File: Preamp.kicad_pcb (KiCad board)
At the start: 2 copper layers, 285 x 74 mm, 169 parts, among them J1 Conn_01x03, J10 RCAJack, J11 XLR4BODYPIN, J12 XLR4BODYPIN, J13 XLR4BODYPIN, J14 RCAJack, J15 RCAJack, J16 RCAJack, J17 RCAJack, J18 RCAJack, J19 RCAJack, J2 Conn_01x02, J20 RCAJack, J21 RCAJack, J22 Jack-DC, J23 Conn_01x02, J24 Conn_01x02, J3 Conn_01x02, J4 RCAJack, J5 RCAJack, J6 Conn_01x01, J7 Conn_01x01, J8 Conn_01x01, J9 Conn_01x01, SW1 SW_SPST, SW2 SW_SPST, SW3 SW_SPST, U1 LM317, U2 LM337, U3 LM4562, U4 LM4562, U5 LM4562, U6 LM4562, U7 LM4562, U8 LM4562

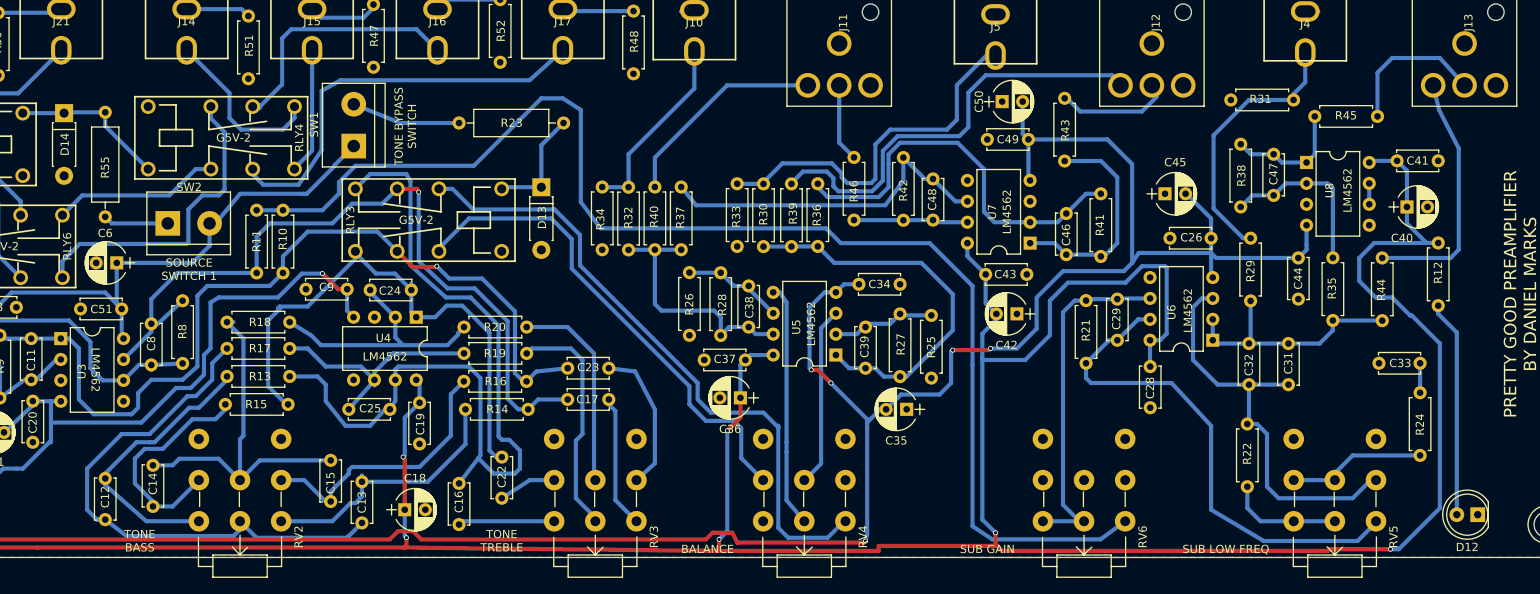
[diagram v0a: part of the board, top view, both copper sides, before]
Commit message: Changed balanced output to THAT1646
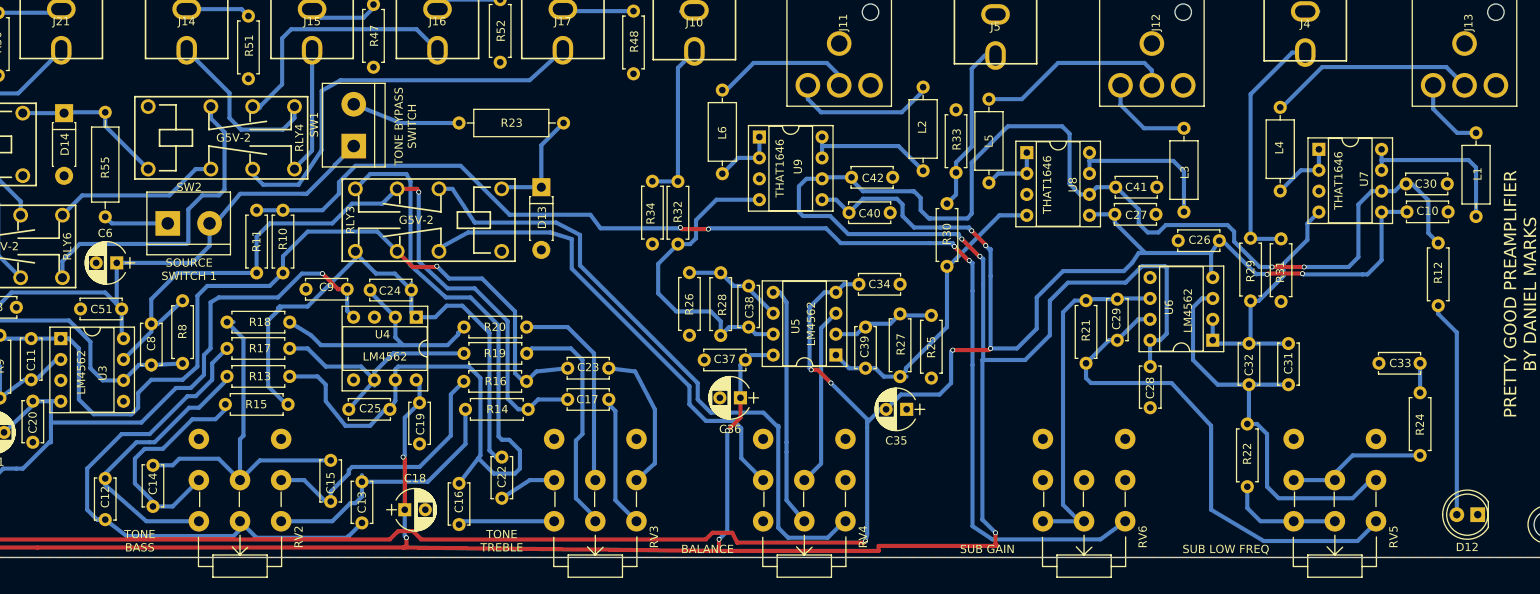
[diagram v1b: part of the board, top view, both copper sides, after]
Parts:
- removed C43, C44, C49: 100 nF, Capacitors_THT:C_Disc_D5.0mm_W2.5mm_P5.00mm
- removed C45, C50: 47 uF, Capacitors_THT:CP_Radial_D5.0mm_P2.50mm
- removed C46, C47, C48: 22 pF, Capacitors_THT:C_Disc_D5.0mm_W2.5mm_P5.00mm
- removed R35, R36, R37, R38, R41, R42: 10k, Resistors_THT:R_Axial_DIN0207_L6.3mm_D2.5mm_P7.62mm_Horizontal
- removed R39, R40, R43, R44, R45, R46: 100R, Resistors_THT:R_Axial_DIN0207_L6.3mm_D2.5mm_P7.62mm_Horizontal
- added C10: 100 nF, Capacitors_THT:C_Disc_D5.0mm_W2.5mm_P5.00mm, F.Cu at (278.0, 64.0)
- added C27: 100 nF, Capacitors_THT:C_Disc_D5.0mm_W2.5mm_P5.00mm, F.Cu at (242.5, 64.3)
- added C30: 100 nF, Capacitors_THT:C_Disc_D5.0mm_W2.5mm_P5.00mm, F.Cu at (277.9, 60.6)
- added L1: FB, Inductors_THT:L_Axial_L7.0mm_D3.3mm_P10.16mm_Horizontal_Fastron_MICC, F.Cu at (281.4, 54.4)
- added L2: FB, Inductors_THT:L_Axial_L7.0mm_D3.3mm_P10.16mm_Horizontal_Fastron_MICC, F.Cu at (214.2, 59.0)
- added L3: FB, Inductors_THT:L_Axial_L7.0mm_D3.3mm_P10.16mm_Horizontal_Fastron_MICC, F.Cu at (245.9, 64.0)
- added L4: FB, Inductors_THT:L_Axial_L7.0mm_D3.3mm_P10.16mm_Horizontal_Fastron_MICC, F.Cu at (257.6, 51.3)
- added L5: FB, Inductors_THT:L_Axial_L7.0mm_D3.3mm_P10.16mm_Horizontal_Fastron_MICC, F.Cu at (222.2, 50.3)
- added L6: FB, Inductors_THT:L_Axial_L7.0mm_D3.3mm_P10.16mm_Horizontal_Fastron_MICC, F.Cu at (189.8, 49.2)
- added U9: THAT1646, Housings_DIP:DIP-8_W7.62mm_Socket, F.Cu at (194.3, 54.9)
- C40, C42: value 47 uF -> 100 nF; footprint Capacitors_THT:CP_Radial_D5.0mm_P2.50mm -> Capacitors_THT:C_Disc_D5.0mm_W2.5mm_P5.00mm
- U3, U4, U5, U6: footprint Housings_DIP:DIP-8_W7.62mm -> Housings_DIP:DIP-8_W7.62mm_Socket
- U7, U8: value LM4562 -> THAT1646; footprint Housings_DIP:DIP-8_W7.62mm -> Housings_DIP:DIP-8_W7.62mm_Socket
- moved C40 62.8 mm to (210.2, 64.1), turned to 180 degrees
- moved U7 36.9 mm to (262.3, 56.4), turned to 0 degrees
- moved U8 34.0 mm to (226.8, 56.8)
- moved R33 31.4 mm to (218.2, 51.6), turned to 270 degrees
- moved C41 29.4 mm to (242.6, 61.0), turned to 180 degrees
- moved R31 25.2 mm to (257.7, 74.9), turned to 90 degrees
- moved C42 22.4 mm to (210.5, 59.8)
- moved R30 22.4 mm to (217.1, 63.0)
- moved R34 6.14 mm to (181.3, 67.9)
- moved R32 6.04 mm to (184.4, 60.3)
- moved C26 1.04 mm to (245.2, 67.5)
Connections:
- C40 pad 1: +15V -> GND
- C40 pad 2: GND -> -15V
- C41 pad 1: +15V -> GND
- C41 pad 2: GND -> +15V
- U7 pad 1: Net-(C46-Pad1) -> Net-(L4-Pad2)
- U7 pad 2: Net-(C46-Pad2) -> Net-(L4-Pad2)
- U7 pad 4: -15V -> Net-(C31-Pad1)
- U7 pad 5: GND -> -15V
- U7 pad 6: Net-(C48-Pad2) -> +15V
- U7 pad 7: Net-(C48-Pad1) -> Net-(L1-Pad2)
- U7 pad 8: +15V -> Net-(L1-Pad2)
- U8 pad 1: Net-(C47-Pad1) -> Net-(L5-Pad2)
- U8 pad 2: Net-(C47-Pad2) -> Net-(L5-Pad2)
- U8 pad 4: -15V -> Net-(C39-Pad1)
- U8 pad 5: GND -> -15V
- U8 pad 6: Net-(U8-Pad6) -> +15V
- U8 pad 7: Net-(U8-Pad6) -> Net-(L3-Pad1)
- U8 pad 8: +15V -> Net-(L3-Pad1)
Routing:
- net Net-(C46-Pad2): track 48.9 -> 0.00 mm
- net Net-(C48-Pad2): track 42.7 -> 0.00 mm
- net Net-(J12-Pad2): track 53.4 -> 11.3 mm
- net Net-(C46-Pad1): track 27.2 -> 0.00 mm
- net Net-(J5-Pad2): track 45.2 -> 22.3 mm
- net +15V: track 552.6 -> 574.5 mm, vias 7 -> 10
- net Net-(C47-Pad2): track 21.6 -> 0.00 mm
- net Net-(J13-Pad2): track 30.8 -> 9.29 mm
- net Net-(L1-Pad2): track 0.00 -> 20.4 mm
- net -15V: track 484.6 -> 504.9 mm, vias 8 -> 12
- net Net-(L3-Pad1): track 0.00 -> 19.5 mm
- net Net-(L2-Pad1): track 0.00 -> 16.1 mm
- net Net-(C47-Pad1): track 14.9 -> 0.00 mm
- net Net-(C48-Pad1): track 13.9 -> 0.00 mm
- net Net-(R10-Pad1): track 158.5 -> 147.1 mm, vias 0 -> 4
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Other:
- board text added: "THAT1646"

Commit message: Changed one input to be balanced
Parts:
- removed R48, R52: 10R, Resistors_THT:R_Axial_DIN0207_L6.3mm_D2.5mm_P7.62mm_Horizontal
- added C43: 100 nF, Capacitors_THT:C_Disc_D5.0mm_W2.5mm_P5.00mm, F.Cu at (186.1, 51.3)
- added C44: 100 nF, Capacitors_THT:C_Disc_D5.0mm_W2.5mm_P5.00mm, F.Cu at (214.5, 61.0)
- added C45: 100 nF, Capacitors_THT:C_Disc_D5.0mm_W2.5mm_P5.00mm, F.Cu at (195.9, 66.0)
- added C46: 100 nF, Capacitors_THT:C_Disc_D5.0mm_W2.5mm_P5.00mm, F.Cu at (191.5, 66.4)
- added C47: 220 uF, Capacitors_THT:CP_Radial_D7.5mm_P2.50mm, F.Cu at (177.1, 63.6)
- added C48: 220 uF, Capacitors_THT:CP_Radial_D7.5mm_P2.50mm, F.Cu at (197.6, 61.6)
- added C49: 47 uF, Capacitors_THT:CP_Radial_D5.0mm_P2.50mm, F.Cu at (95.8, 81.8)
- added C50: 47 uF, Capacitors_THT:CP_Radial_D5.0mm_P2.50mm, F.Cu at (87.3, 82.6)
- added C52: 47 uF, Capacitors_THT:CP_Radial_D5.0mm_P2.50mm, F.Cu at (87.4, 79.3)
- added C53: 47 uF, Capacitors_THT:CP_Radial_D5.0mm_P2.50mm, F.Cu at (95.8, 78.5)
- added C54: 100 pF, Capacitors_THT:C_Disc_D5.0mm_W2.5mm_P5.00mm, F.Cu at (144.5, 54.4)
- added C55: 100 pF, Capacitors_THT:C_Disc_D5.0mm_W2.5mm_P5.00mm, F.Cu at (168.5, 43.4)
- added C56: 100 pF, Capacitors_THT:C_Disc_D5.0mm_W2.5mm_P5.00mm, F.Cu at (152.9, 54.5)
- added C57: 100 pF, Capacitors_THT:C_Disc_D5.0mm_W2.5mm_P5.00mm, F.Cu at (165.4, 43.4)
- added J25: Conn_01x01, Connectors:1pin, F.Cu at (236.3, 54.4)
- added J26: Conn_01x01, Connectors:1pin, F.Cu at (185.0, 98.0)
- added J27: Conn_01x01, Connectors:1pin, F.Cu at (114.5, 49.0)
- added J28: Conn_01x01, Connectors:1pin, F.Cu at (107.0, 98.0)
- added JP1: INA134, Pin_Headers:Pin_Header_Straight_1x02_Pitch2.54mm, F.Cu at (179.1, 56.5)
- added JP2: INA134, Pin_Headers:Pin_Header_Straight_1x02_Pitch2.54mm, F.Cu at (199.5, 54.3)
- added R35: 10k, Resistors_THT:R_Axial_DIN0207_L6.3mm_D2.5mm_P7.62mm_Horizontal, F.Cu at (87.0, 102.5)
- added R36: 10k, Resistors_THT:R_Axial_DIN0207_L6.3mm_D2.5mm_P7.62mm_Horizontal, F.Cu at (94.5, 99.2)
- added U10: THAT1200, Housings_DIP:DIP-8_W7.62mm_Socket, F.Cu at (191.0, 63.4)
- added U11: THAT1200, Housings_DIP:DIP-8_W7.62mm_Socket, F.Cu at (211.1, 64.7)
- J16, J17: value RCAJack -> XLR4BODYPIN; footprint Preamp:RCAConnectorCommon -> Preamp:IOXLR3FEH
- R8, R9: value 22k -> 47k
- moved SW1 40.2 mm to (180.6, 74.6), turned to 180 degrees
- moved R32 36.6 mm to (220.9, 57.6)
- moved R34 36.5 mm to (217.8, 65.3)
- moved R30 32.3 mm to (248.9, 57.7)
- moved U9 31.1 mm to (225.1, 59.1)
- moved C40 30.8 mm to (241.0, 64.9)
- moved R33 30.7 mm to (245.8, 65.2), turned to 90 degrees
- moved C42 30.6 mm to (241.0, 61.6)
- moved L4 29.1 mm to (277.7, 72.3), turned to 180 degrees
- moved R23 29.0 mm to (182.4, 68.5), turned to 180 degrees
- moved U8 28.7 mm to (255.5, 58.4)
- moved C41 28.6 mm to (271.1, 62.8)
- moved C27 28.5 mm to (271.0, 65.9)
- moved L6 28.5 mm to (217.8, 54.2), turned to 0 degrees
- moved R29 26.6 mm to (280.6, 68.3), turned to 180 degrees
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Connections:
- C3 pad 1: LEFTIN -> Net-(C3-Pad1)
- C7 pad 1: RIGHTIN -> Net-(C50-Pad2)
- J16 pad 1: Net-(J16-Pad1) -> GND
- J16 pad 2: Net-(J16-Pad2) -> Net-(C56-Pad2)
- J17 pad 1: Net-(J17-Pad1) -> GND
- J17 pad 2: Net-(J17-Pad2) -> Net-(C57-Pad2)
- RLY4 pad 1: GND -> Net-(D14-Pad1)
- RLY4 pad 3: Net-(J16-Pad2) -> Net-(J14-Pad2)
- RLY4 pad 4: Net-(J14-Pad2) -> Net-(JP1-Pad1)
- RLY4 pad 5: Net-(D14-Pad1) -> GND
- RLY4 pad 7: Net-(J17-Pad2) -> Net-(J15-Pad2)
- RLY4 pad 8: Net-(J15-Pad2) -> Net-(JP2-Pad1)
- RV1 pad 1: LEFTIN -> Net-(R35-Pad1)
- RV1 pad 4: RIGHTIN -> Net-(R36-Pad2)
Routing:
- net -15V: track 504.9 -> 713.4 mm, vias 12 -> 7
- net +15V: track 574.5 -> 753.9 mm, vias 10 -> 8
- net Net-(JP2-Pad1): track 0.00 -> 109.5 mm
- net Net-(C54-Pad2): track 0.00 -> 62.2 mm
- net Net-(JP1-Pad1): track 0.00 -> 62.1 mm
- net Net-(C57-Pad2): track 0.00 -> 60.7 mm
- net Net-(C55-Pad2): track 0.00 -> 59.0 mm
- net Net-(J17-Pad2): track 50.1 -> 0.00 mm
- net Net-(C56-Pad2): track 0.00 -> 48.9 mm
- net Net-(C3-Pad1): track 0.00 -> 39.2 mm
- net Net-(C38-Pad1): track 38.7 -> 71.7 mm
- net Net-(J16-Pad2): track 31.4 -> 0.00 mm
- net LEFTIN: track 36.4 -> 6.16 mm
- net Net-(C39-Pad1): track 37.7 -> 63.9 mm
- net Net-(C50-Pad2): track 0.00 -> 23.8 mm
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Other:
- board text added: "1"
- board text added: "THAT1206"

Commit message: Before changing RCA jacks
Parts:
- moved C55 17.6 mm to (185.9, 41.4)
- moved C57 11.2 mm to (165.4, 54.6), turned to 90 degrees
- moved R51 10.8 mm to (108.0, 48.0), turned to 180 degrees
- moved J16 4.32 mm to (151.4, 39.5)
- moved J15 2.40 mm to (134.1, 40.3)
- moved R47 2.28 mm to (126.8, 39.9)
- moved J17 1.86 mm to (175.8, 39.6)
- moved J20 1.85 mm to (89.2, 40.3)
- moved R50 1.85 mm to (96.8, 39.8)
- moved J21 1.80 mm to (103.9, 40.3)
- moved R54 1.76 mm to (81.8, 38.9)
- moved J14 1.60 mm to (118.8, 40.3)
- moved R49 1.55 mm to (66.2, 39.6)
- moved J19 1.40 mm to (73.7, 40.4)
- moved J18 1.01 mm to (58.4, 40.6)
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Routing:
- net Net-(C55-Pad2): track 59.0 -> 50.5 mm
- net Net-(J14-Pad1): track 12.7 -> 17.6 mm
- net Net-(J14-Pad2): track 19.6 -> 23.1 mm
- net Net-(C54-Pad2): track 62.2 -> 65.4 mm
- net Net-(C56-Pad2): track 48.9 -> 51.6 mm
- net Net-(JP2-Pad1): track 109.5 -> 110.9 mm
- net Net-(J15-Pad2): track 17.9 -> 16.8 mm
- net Net-(JP1-Pad1): track 62.1 -> 63.1 mm
- net Net-(J18-Pad2): track 35.8 -> 36.8 mm
- net Net-(J21-Pad2): track 19.6 -> 18.6 mm
- net Net-(J20-Pad2): track 19.6 -> 18.7 mm
- net Net-(J19-Pad2): track 15.4 -> 16.1 mm
- net Net-(J19-Pad1): track 7.57 -> 8.20 mm
- net Net-(C57-Pad2): track 60.7 -> 60.1 mm
- net Net-(J15-Pad1): track 9.61 -> 9.05 mm

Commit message: JLCPCB 2021-03-26
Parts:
- RV1: footprint Preamp:Dual_Potentiometer_Switch_WirePads -> Preamp:Dual_Potentiometer_Switch_Wide_WirePads
- moved C55 5.78 mm to (185.8, 47.2), turned to 90 degrees
- moved C54 5.10 mm to (149.6, 54.4), turned to 180 degrees
- moved RV1 5.08 mm to (76.2, 101.6)
- moved C43 1.76 mm to (187.8, 51.5)
- moved J16 1.66 mm to (153.0, 40.0)
- moved J17 1.53 mm to (177.3, 39.9)
- moved J12 1.51 mm to (247.0, 41.0)
- moved U1 1.35 mm to (52.5, 96.2)
- moved J11 1.12 mm to (211.0, 41.0)
- moved U2 0.57 mm to (41.8, 84.3)
- moved C21 0.25 mm to (101.8, 93.3)
- moved C56 0.15 mm to (152.9, 54.3)
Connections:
- C54 pad 1: GND -> Net-(C54-Pad1)
- C54 pad 2: Net-(C54-Pad2) -> GND
- C55 pad 1: GND -> Net-(C55-Pad1)
- C55 pad 2: Net-(C55-Pad2) -> GND
- J16 pad 3: Net-(C54-Pad2) -> Net-(C54-Pad1)
- J17 pad 3: Net-(C55-Pad2) -> Net-(C55-Pad1)
- U10 pad 2: Net-(C56-Pad2) -> Net-(C54-Pad1)
- U10 pad 3: Net-(C54-Pad2) -> Net-(C56-Pad2)
- U11 pad 2: Net-(C57-Pad2) -> Net-(C55-Pad1)
- U11 pad 3: Net-(C55-Pad2) -> Net-(C57-Pad2)
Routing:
- net Net-(C54-Pad2): track 65.4 -> 0.00 mm
- net Net-(C54-Pad1): track 0.00 -> 58.3 mm
- net Net-(C55-Pad2): track 50.5 -> 0.00 mm
- net Net-(C55-Pad1): track 0.00 -> 44.9 mm
- net Net-(JP2-Pad1): track 110.9 -> 103.2 mm
- net Net-(L4-Pad2): track 10.9 -> 7.54 mm
- net Net-(C57-Pad2): track 60.1 -> 63.1 mm
- net Net-(J19-Pad2): track 16.1 -> 18.8 mm
- net Net-(J14-Pad1): track 17.6 -> 14.8 mm
- net Net-(J20-Pad1): track 7.74 -> 10.2 mm
- net Net-(J18-Pad1): track 7.87 -> 10.3 mm
- net Net-(J19-Pad1): track 8.20 -> 10.4 mm
- net Net-(JP1-Pad1): track 63.1 -> 65.3 mm
- net +15V: track 753.9 -> 752.0 mm
- net Net-(J21-Pad1): track 7.33 -> 9.17 mm
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
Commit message: Pre off relay
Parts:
- removed R23, R55, R56, R57: 150R, Resistors_THT:R_Axial_DIN0309_L9.0mm_D3.2mm_P12.70mm_Horizontal
- added R37: NC, Resistors_THT:R_Axial_DIN0207_L6.3mm_D2.5mm_P7.62mm_Horizontal, F.Cu at (94.7, 92.1)
- added R38: NC, Resistors_THT:R_Axial_DIN0207_L6.3mm_D2.5mm_P7.62mm_Horizontal, F.Cu at (86.8, 85.7)
- added R39: NC, Resistors_THT:R_Axial_DIN0207_L6.3mm_D2.5mm_P7.62mm_Horizontal, F.Cu at (200.1, 87.1)
- added R40: NC, Resistors_THT:R_Axial_DIN0207_L6.3mm_D2.5mm_P7.62mm_Horizontal, F.Cu at (211.8, 95.3)
- added R41: 100R, Resistors_THT:R_Axial_DIN0411_L9.9mm_D3.6mm_P12.70mm_Horizontal, F.Cu at (80.4, 76.0)
- added R42: 100R, Resistors_THT:R_Axial_DIN0411_L9.9mm_D3.6mm_P12.70mm_Horizontal, F.Cu at (74.6, 65.6)
- R10, R11: value 10k -> 47k
- R2, R7: value 10k -> 4k7
- R5, R6: value 470R -> 560R
- moved J27 28.6 mm to (142.4, 47.2)
- moved C50 7.86 mm to (79.6, 81.3), turned to 0 degrees
- moved D11 7.80 mm to (19.4, 72.6), turned to 90 degrees
- moved C36 6.03 mm to (188.1, 91.2)
- moved RLY4 5.00 mm to (116.6, 55.7)
- moved C7 3.82 mm to (85.5, 82.5), turned to 0 degrees
- moved SW3 2.81 mm to (80.2, 51.8)
- moved R7 2.61 mm to (94.8, 88.9)
- moved C52 1.57 mm to (86.6, 78.0)
- moved R2 0.56 mm to (94.6, 95.4)
- moved R36 0.38 mm to (94.7, 99.6)
- moved R35 0.32 mm to (87.1, 102.8)
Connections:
- C26 pad 1: GND -> -15V
- C26 pad 2: -15V -> GND
- D11 pad 1: GND -> Net-(D11-Pad1)
- D11 pad 2: Net-(D11-Pad2) -> GND
- D16 pad 2: Net-(D16-Pad2) -> -15V
- J3 pad 2: Net-(D11-Pad2) -> Net-(D11-Pad1)
- RLY2 pad 5: Net-(D11-Pad2) -> Net-(D11-Pad1)
- RLY7 pad 5: Net-(D16-Pad2) -> -15V
- RV1 pad 8: Net-(D11-Pad2) -> Net-(D11-Pad1)
- SW1 pad 2: Net-(R23-Pad1) -> Net-(D13-Pad1)
- SW2 pad 1: Net-(R55-Pad1) -> Net-(D14-Pad1)
- SW3 pad 1: Net-(R56-Pad1) -> Net-(D15-Pad2)
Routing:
- net Net-(D11-Pad2): track 101.4 -> 0.00 mm
- net Net-(D11-Pad1): track 0.00 -> 101.4 mm
- net +15V: track 752.0 -> 778.2 mm
- net Net-(D15-Pad2): track 12.7 -> 29.4 mm
- net Net-(R40-Pad1): track 29.7 -> 45.0 mm
- net Net-(D14-Pad1): track 16.6 -> 31.2 mm
- net Net-(R40-Pad2): track 77.5 -> 91.1 mm
- net Net-(R23-Pad1): track 12.0 -> 0.00 mm
- net -15V: track 714.4 -> 702.6 mm
- net Net-(D13-Pad1): track 12.8 -> 23.5 mm
- net Net-(R56-Pad1): track 10.2 -> 0.00 mm
- net Net-(D16-Pad2): track 9.56 -> 0.00 mm
- net Net-(J14-Pad2): track 23.1 -> 14.2 mm
- net Net-(R55-Pad1): track 7.80 -> 0.00 mm
- net Net-(R38-Pad1): track 15.6 -> 22.7 mm
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
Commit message: Tried a relay version out
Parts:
- removed R41, R42: 100R, Resistors_THT:R_Axial_DIN0411_L9.9mm_D3.6mm_P12.70mm_Horizontal
- added R23: 22R, Resistors_THT:R_Axial_DIN0309_L9.0mm_D3.2mm_P12.70mm_Horizontal, F.Cu at (74.0, 66.9)
- added R43: 22R, Resistors_THT:R_Axial_DIN0309_L9.0mm_D3.2mm_P12.70mm_Horizontal, F.Cu at (73.9, 72.1)
- added RLY8: DPDTRelay, Preamp:G2VRelay, F.Cu at (59.2, 84.2)
- C1, C2: value 3300 uF -> 47 uF; footprint Capacitors_THT:CP_Radial_D10.0mm_P5.00mm -> Capacitors_THT:CP_Radial_D7.5mm_P2.50mm
- moved C1 42.9 mm to (60.4, 98.6), turned to 270 degrees
- moved R5 18.9 mm to (45.1, 83.0), turned to 270 degrees
- moved C4 18.1 mm to (51.0, 88.0)
- moved D5 17.7 mm to (21.7, 92.3), turned to 180 degrees
- moved D7 15.9 mm to (40.3, 90.3), turned to 90 degrees
- moved RLY1 13.6 mm to (26.5, 62.8), turned to 90 degrees
- moved D6 13.2 mm to (21.7, 95.8), turned to 180 degrees
- moved R4 12.6 mm to (42.4, 51.1), turned to 270 degrees
- moved U2 12.1 mm to (44.9, 72.7), turned to 180 degrees
- moved R3 9.63 mm to (56.7, 93.0)
- moved R6 8.40 mm to (35.7, 65.3), turned to 0 degrees
- moved D2 8.17 mm to (31.0, 92.3), turned to 270 degrees
- moved RLY5 6.94 mm to (109.3, 55.1)
- moved D14 6.25 mm to (116.0, 51.2)
- moved RLY4 6.05 mm to (122.6, 54.9)
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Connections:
- RLY2 pad 2: Net-(D9-Pad2) -> Net-(D10-Pad2)
- RLY2 pad 4: Net-(D5-Pad2) -> Net-(D2-Pad2)
- RLY2 pad 6: Net-(D10-Pad2) -> Net-(D9-Pad2)
- RLY2 pad 8: Net-(D2-Pad2) -> Net-(D5-Pad2)
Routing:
- net Net-(D2-Pad2): track 33.7 -> 66.1 mm
- net Net-(D5-Pad2): track 33.9 -> 62.3 mm
- net Net-(D4-Pad2): track 62.5 -> 38.6 mm, vias 0 -> 1
- net Net-(R43-Pad1): track 0.00 -> 21.6 mm
- net Net-(D10-Pad2): track 55.6 -> 74.6 mm
- net Net-(C2-Pad2): track 67.5 -> 83.5 mm
- net Net-(R23-Pad1): track 0.00 -> 15.4 mm
- net +15V: track 778.2 -> 763.8 mm, vias 8 -> 9
- net Net-(D1-Pad2): track 19.8 -> 30.8 mm, vias 0 -> 1
- net Net-(C1-Pad1): track 47.5 -> 57.9 mm
- net Net-(J3-Pad1): track 102.3 -> 110.7 mm
- net Net-(D11-Pad1): track 101.4 -> 109.4 mm
- net Net-(J19-Pad2): track 18.8 -> 26.5 mm
- net Net-(JP1-Pad1): track 69.3 -> 61.9 mm
- net Net-(J21-Pad2): track 18.6 -> 11.5 mm
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
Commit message: Put larger capacitors on
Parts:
- removed RLY8: DPDTRelay, Preamp:G2VRelay
- C1, C2: value 47 uF -> 1500 uF; footprint Capacitors_THT:CP_Radial_D7.5mm_P2.50mm -> Capacitors_THT:CP_Radial_D10.0mm_P5.00mm
- R10, R11, R8, R9: value 47k -> 22k
- R23, R43: value 22R -> 75R
- moved R23 19.3 mm to (61.0, 81.1)
- moved R43 18.5 mm to (60.9, 85.2)
- moved D16 17.7 mm to (79.1, 68.6), turned to 90 degrees
- moved C5 8.00 mm to (64.9, 74.3)
- moved R4 7.74 mm to (46.1, 57.9)
- moved R3 4.10 mm to (56.6, 88.9)
- moved RLY7 3.81 mm to (69.5, 65.8)
- moved C1 3.31 mm to (60.7, 95.3)
- moved J23 3.30 mm to (59.1, 55.8)
- moved SW3 3.14 mm to (83.3, 52.3)
- moved J24 3.11 mm to (59.0, 67.0)
- moved C2 3.05 mm to (38.9, 51.8)
- moved J22 1.30 mm to (43.5, 46.3)
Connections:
- R23 pad 1: Net-(R23-Pad1) -> -15V
- R43 pad 1: Net-(R43-Pad1) -> +15V
- U6 pad 3: Net-(C31-Pad2) -> Net-(C33-Pad2)
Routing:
- net Net-(C33-Pad2): track 3.98 -> 44.2 mm
- net Net-(R43-Pad1): track 21.6 -> 0.00 mm
- net Net-(C31-Pad2): track 51.5 -> 33.4 mm
- net Net-(R23-Pad1): track 15.4 -> 0.00 mm
- net -15V: track 703.9 -> 692.8 mm
- net Net-(R4-Pad2): track 18.8 -> 10.5 mm
- net Net-(J22-Pad1): track 17.1 -> 21.6 mm
- net (no net): track 0.00 -> 1.27 mm
- net Net-(C1-Pad1): track 57.9 -> 56.7 mm
- net Net-(J24-Pad1): track 16.7 -> 17.8 mm
- net Net-(C2-Pad2): track 83.5 -> 82.4 mm
- net Net-(J24-Pad2): track 25.2 -> 24.2 mm
- net +15V: track 763.8 -> 764.6 mm
- net Net-(J22-Pad2): track 36.9 -> 36.2 mm
- net Net-(J23-Pad2): track 6.19 -> 6.73 mm
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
